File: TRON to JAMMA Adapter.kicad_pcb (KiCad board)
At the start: 2 copper layers, 111 x 98.7 mm, 59 parts, among them P1 1K, P2 10K, P3 1K, U1 74LS86, U2A 74LS191, U2B 74LS191, U3 NE555, U4 LM386, U5 NE555

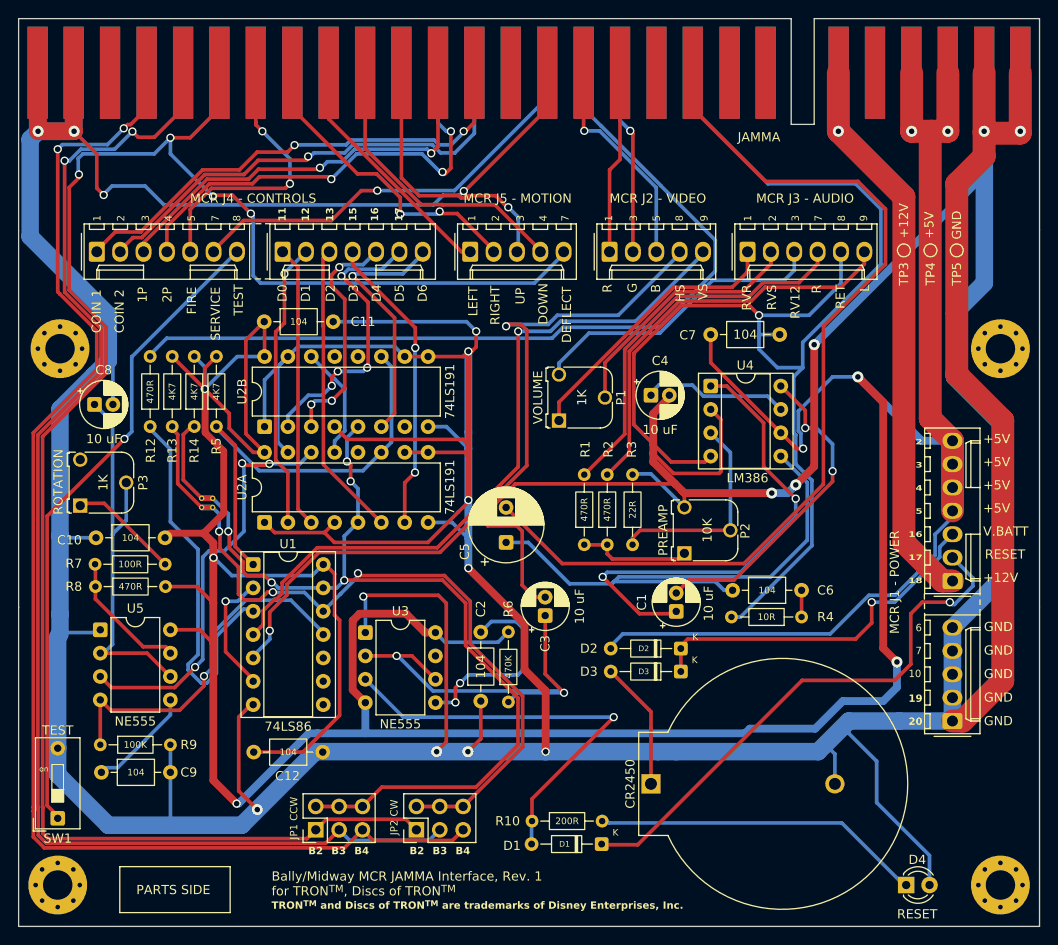
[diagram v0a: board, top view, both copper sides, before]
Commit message: Use 3.96mm header for J1
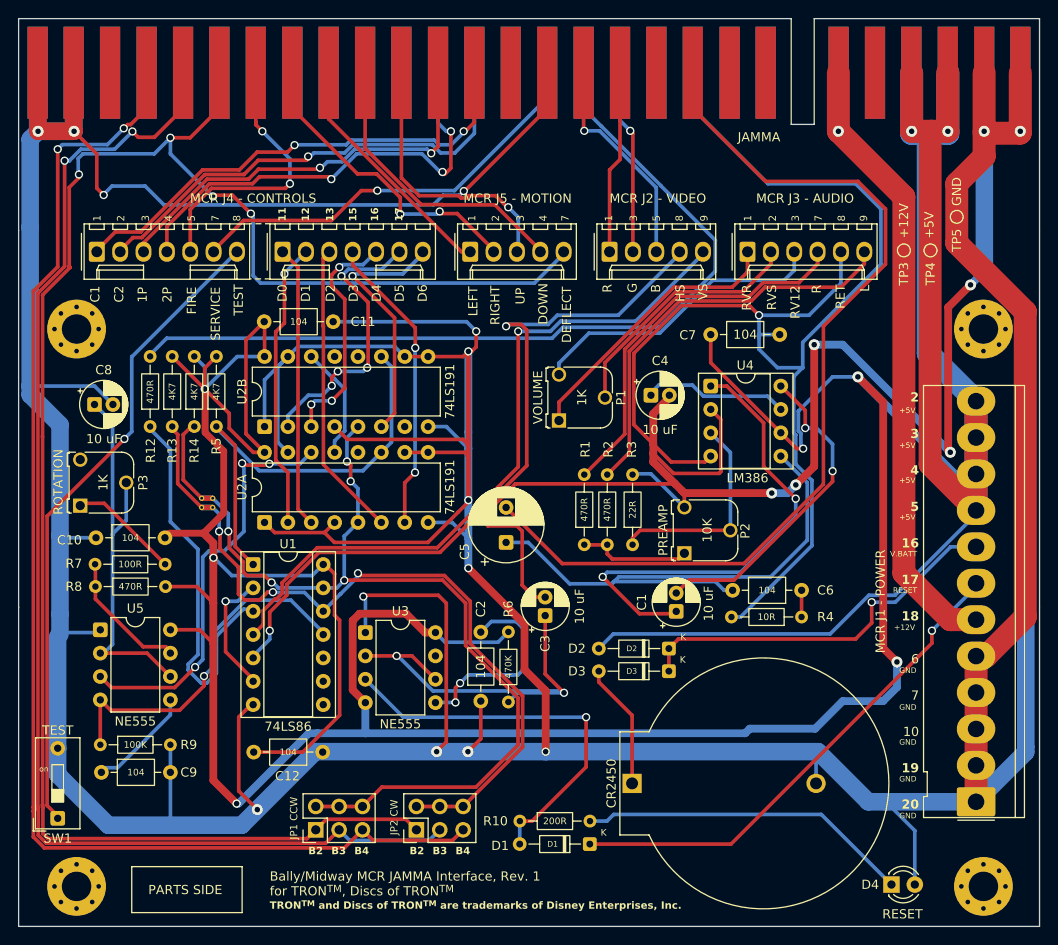
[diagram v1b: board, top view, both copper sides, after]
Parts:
- removed MCRJ1A: Molex_KK-254_AE-6410-05A_1x05_P2.54mm_Vertical, Connector_Molex:Molex_KK-254_AE-6410-05A_1x05_P2.54mm_Vertical
- MCRJ1: renamed from MCRJ1B; value Molex_KK-254_AE-6410-07A_1x07_P2.54mm_Vertical -> Molex_KK-396_5273-12A_1x12_P3.96mm_Vertical; footprint Connector_Molex:Molex_KK-254_AE-6410-07A_1x07_P2.54mm_Vertical -> Connector_Molex:Molex_KK-396_5273-12A_1x12_P3.96mm_Vertical
- moved MCRJ1 24.1 mm to (193.6, 130.2)
- moved GND 3.65 mm to (191.5, 66.6)
- moved PMH1 2.83 mm to (194.4, 78.8)
- moved PMH4 2.79 mm to (95.8, 78.8)
- moved PMH3 2.06 mm to (95.8, 139.4)
- moved CR2450 2.05 mm to (156.2, 128.2)
- moved PMH2 1.86 mm to (194.4, 139.4)
- moved D4 1.60 mm to (184.4, 139.2)
- moved R10 1.32 mm to (144.0, 132.3)
- moved D3 1.30 mm to (160.2, 116.0)
- moved D2 1.30 mm to (160.2, 113.5)
- moved D1 1.29 mm to (151.6, 134.8)
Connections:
- MCRJ1 pad 1: +12V_IN -> GND
- MCRJ1 pad 2: RESET_5V_OUT -> GND
- MCRJ1 pad 3: V.BATT -> GND
- MCRJ1 pad 4: +5V -> GND
- MCRJ1 pad 5: +5V -> GND
- MCRJ1 pad 6: +5V -> +12V_IN
- MCRJ1 pad 7: +5V -> RESET_5V_OUT
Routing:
- net +5V: track 466.1 -> 528.5 mm
- net GND: track 1007.7 -> 1057.2 mm, vias 19 -> 21
- net +12V_IN: track 67.9 -> 74.2 mm
- net RESET_5V_OUT: track 59.5 -> 54.7 mm
- net 1P_B4: track 143.8 -> 140.3 mm
- net 1P_B3: track 143.6 -> 140.3 mm
- net 1P_B2: track 197.9 -> 194.6 mm
- net RESET_5V: track 46.2 -> 43.3 mm
- net V.BATT: track 39.3 -> 41.8 mm
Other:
- board text added: "C1"
- board text added: "C2"
- board text removed: "COIN 1"
- board text removed: "COIN 2"

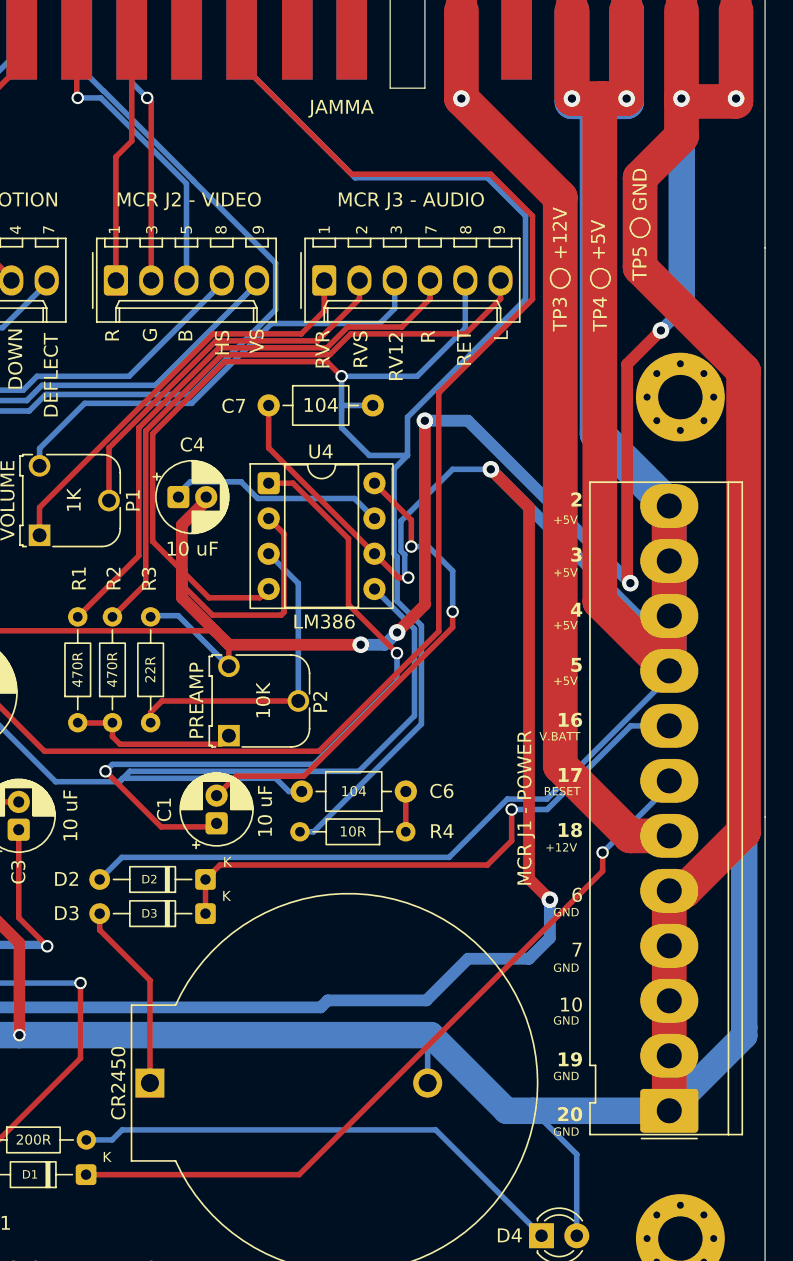
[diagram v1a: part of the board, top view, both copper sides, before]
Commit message: straight 3.96 for Spy Hunter, right angle for Tron
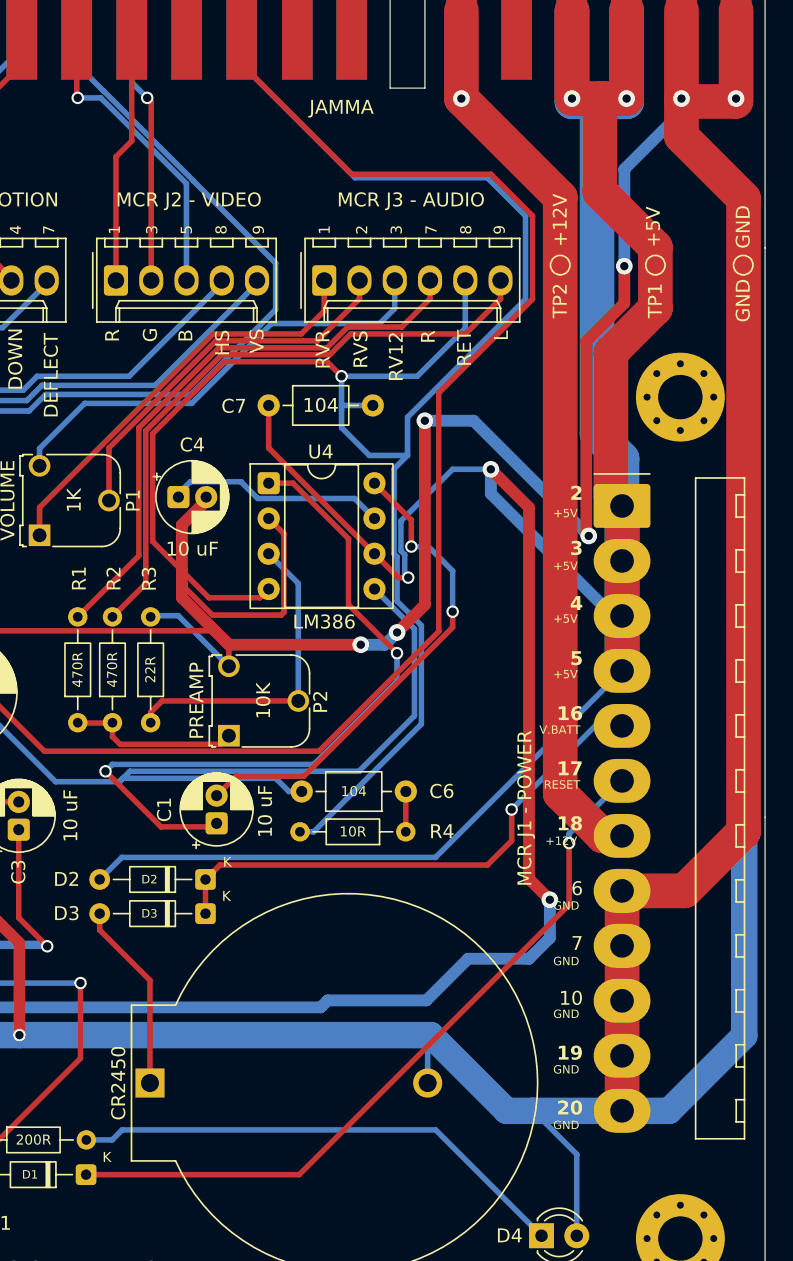
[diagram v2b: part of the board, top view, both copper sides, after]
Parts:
- +12V: value TP3 -> TP2
- +5V: value TP4 -> TP1
- GND: value TP5 -> GND
- MCRJ1: value Molex_KK-396_5273-12A_1x12_P3.96mm_Vertical -> Molex_KK-396_A-41792-0012_1x12_P3.96mm_Horizontal; footprint Connector_Molex:Molex_KK-396_5273-12A_1x12_P3.96mm_Vertical -> Connector_Molex:Molex_KK-396_A-41792-0012_1x12_P3.96mm_Horizontal
- moved MCRJ1 43.7 mm to (190.2, 86.6), turned to -90 degrees
- moved GND 7.90 mm to (198.9, 69.3)
- moved +5V 4.07 mm to (192.6, 69.3)
- moved +12V 0.96 mm to (185.7, 69.3)
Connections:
- MCRJ1 pad 1: GND -> +5V
- MCRJ1 pad 10: +5V -> GND
- MCRJ1 pad 11: +5V -> GND
- MCRJ1 pad 12: +5V -> GND
- MCRJ1 pad 2: GND -> +5V
- MCRJ1 pad 3: GND -> +5V
- MCRJ1 pad 4: GND -> +5V
- MCRJ1 pad 5: GND -> V.BATT
- MCRJ1 pad 6: +12V_IN -> RESET_5V_OUT
- MCRJ1 pad 7: RESET_5V_OUT -> +12V_IN
- MCRJ1 pad 8: V.BATT -> GND
- MCRJ1 pad 9: +5V -> GND
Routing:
- net +5V: track 528.5 -> 510.4 mm
- net GND: track 1057.2 -> 1051.6 mm
- net V.BATT: track 41.8 -> 39.0 mm
- net +12V_IN: track 74.2 -> 72.6 mm
- net RESET_5V_OUT: track 54.7 -> 53.3 mm
